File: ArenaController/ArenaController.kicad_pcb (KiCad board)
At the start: 2 copper layers, 80 x 110 mm, 30 parts, among them J1 RJ45, J2 RJ45, J4 RJ45, J5 RJ45, J6 RJ45, J8 Screw_Terminal_01x04, J9 Barrel_Jack_MountingPin, Q1 FS3400, Q2 FS3400, Q3 FS3400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

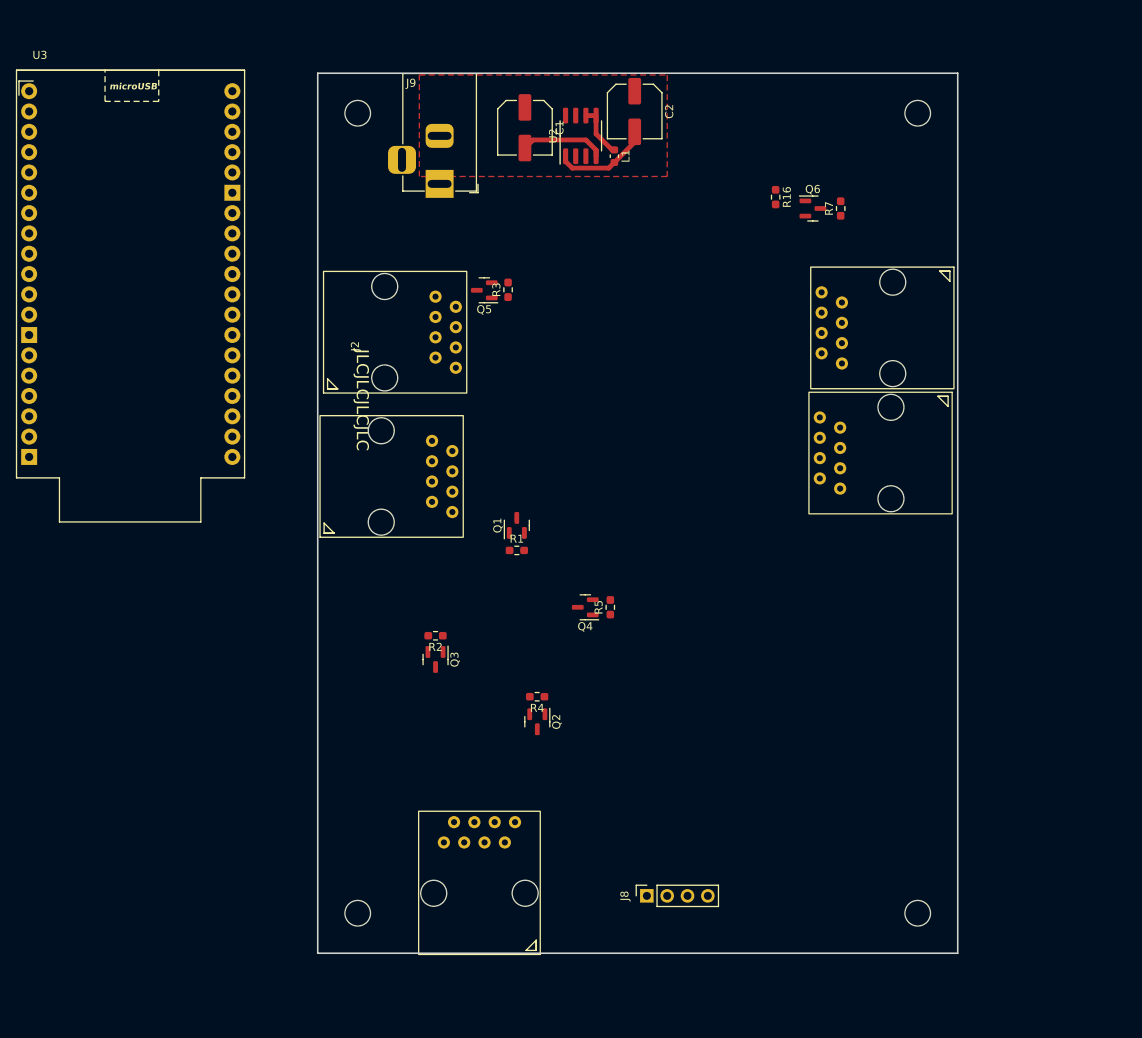
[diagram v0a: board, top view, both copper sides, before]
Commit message: Updated layout, added major routing.  Still need connector for the WS2812B output and pin relayout.
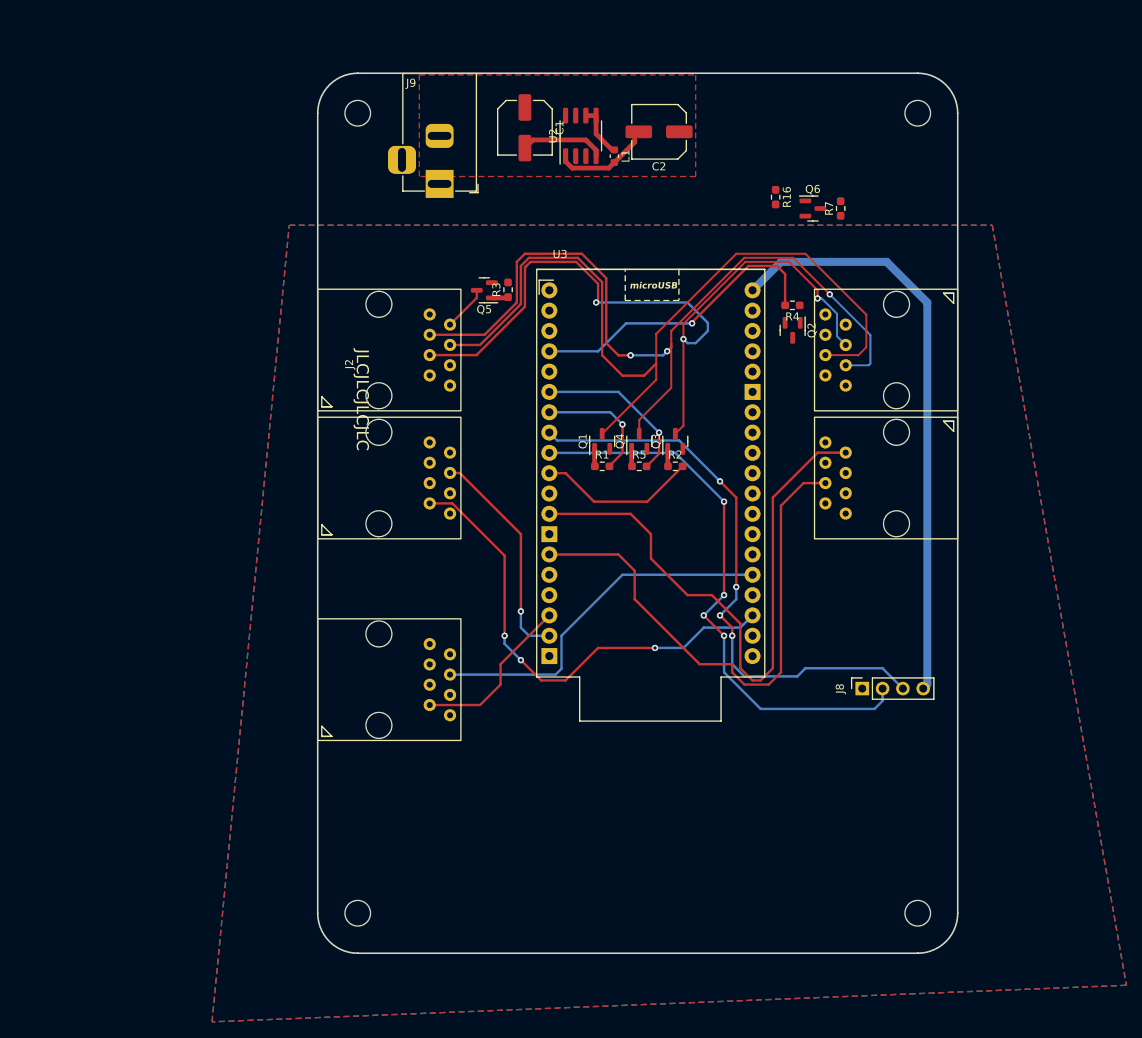
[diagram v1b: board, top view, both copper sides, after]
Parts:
- moved U3 69.6 mm to (136.7, 95.0)
- moved R4 58.4 mm to (154.3, 74.0)
- moved Q2 58.4 mm to (154.4, 77.1)
- moved Q3 40.5 mm to (139.7, 91.0), turned to 90 degrees
- moved J4 38.6 mm to (95.0, 128.4), turned to 90 degrees
- moved J8 37.4 mm to (163.1, 121.9)
- moved R2 36.7 mm to (139.7, 94.1), turned to 0 degrees
- moved kibuzzard-638A219C 36.5 mm to (97.8, 120.3), turned to 90 degrees
- moved Q4 21.8 mm to (135.2, 91.0), turned to 90 degrees
- moved J6 18.8 mm to (175.0, 88.0)
- moved R5 18.0 mm to (135.2, 94.1), turned to 0 degrees
- moved Q1 15.0 mm to (130.6, 91.0)
- moved R1 15.0 mm to (130.6, 94.1)
- moved J1 12.9 mm to (175.0, 72.0)
- moved C2 3.97 mm to (137.7, 52.3), turned to 180 degrees
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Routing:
- net /s_Green: track 0.00 -> 103.7 mm
- net /s_Yellow: track 0.00 -> 102.2 mm, vias 0 -> 3
- net /s_Horn: track 0.00 -> 96.6 mm, vias 0 -> 3
- net /T_A_End: track 0.00 -> 75.0 mm
- net +5V: track 12.3 -> 86.2 mm
- net /Dis_serial_Rx: track 0.00 -> 72.5 mm, vias 0 -> 4
- net /Dis_Serial_Tx: track 0.00 -> 71.5 mm, vias 0 -> 4
- net /T_A_Start: track 0.00 -> 66.5 mm
- net /T_B_Start: track 0.00 -> 59.3 mm, vias 0 -> 3
- net /G_Start: track 0.00 -> 45.4 mm
- net /m_Red_1: track 0.00 -> 38.3 mm, vias 0 -> 1
- net /T_B_End: track 0.00 -> 27.7 mm, vias 0 -> 1
- net /G_End: track 0.00 -> 21.1 mm
- net /m_Yellow: track 0.00 -> 20.7 mm, vias 0 -> 1
- net /m_Horn: track 0.00 -> 20.0 mm
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- added copper zone on B.Cu, net GND
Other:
- outline, holes or cut-outs redrawn

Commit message: Tiny cleanup, workable version, yay.
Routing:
- net +12V: track 10.6 -> 115.4 mm
- net +5V: track 86.2 -> 111.1 mm, vias 0 -> 1
- net /m_Red_2: track 0.00 -> 16.6 mm, vias 0 -> 1
- net /s_Green: track 103.7 -> 93.3 mm, vias 0 -> 2
- net /s_Horn: track 96.6 -> 90.8 mm, vias 3 -> 2
- net /m_Red_1: track 38.3 -> 42.5 mm, vias 1 -> 0
- net /s_Yellow: track 102.2 -> 98.7 mm, vias 3 -> 2
- net /m_Horn: track 20.0 -> 17.0 mm
- added copper zone on F.Cu, net +12V

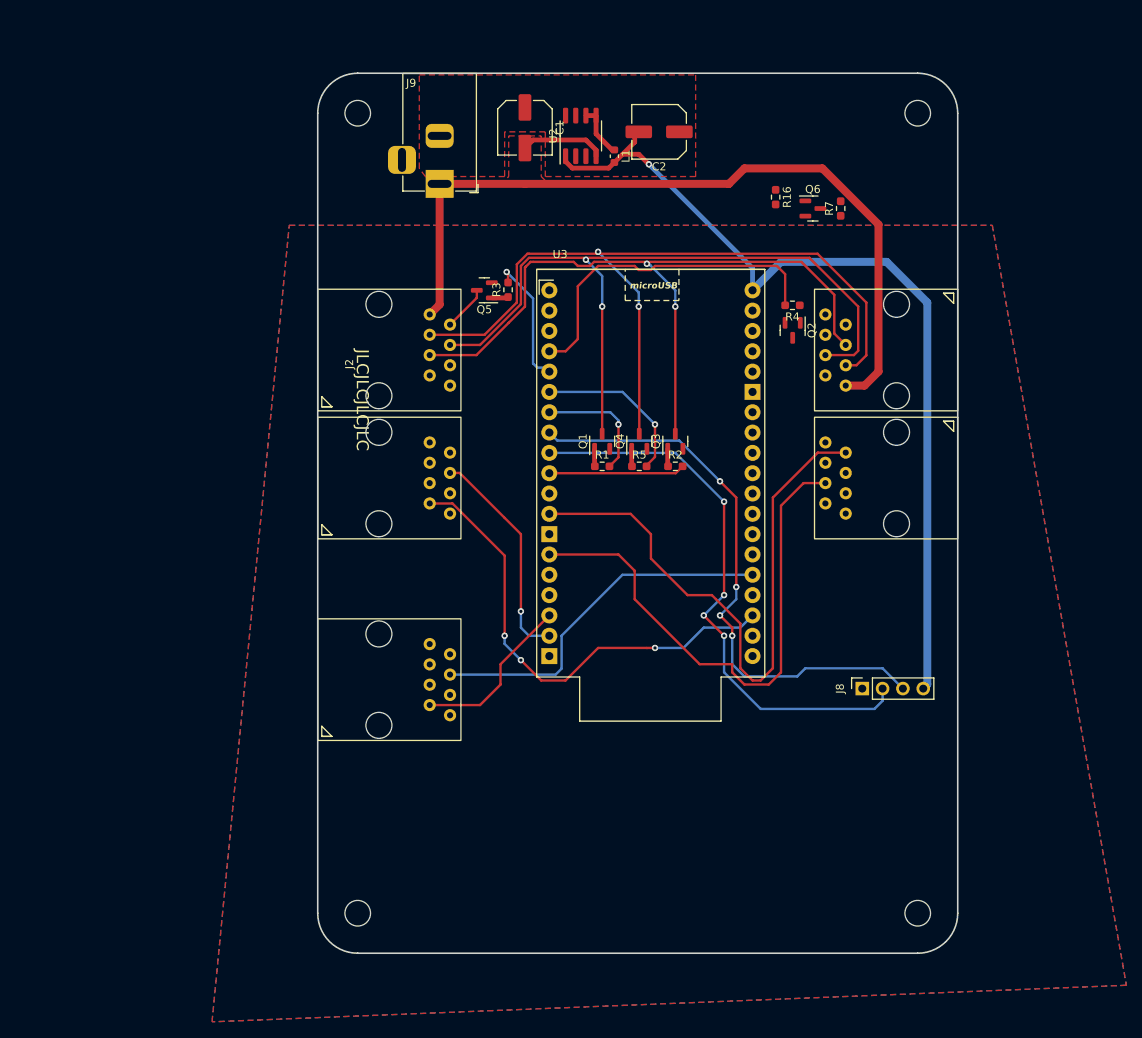
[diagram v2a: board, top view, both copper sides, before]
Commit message: Revision .4 layout with a sane ground plane, do fix the footprint shit tho
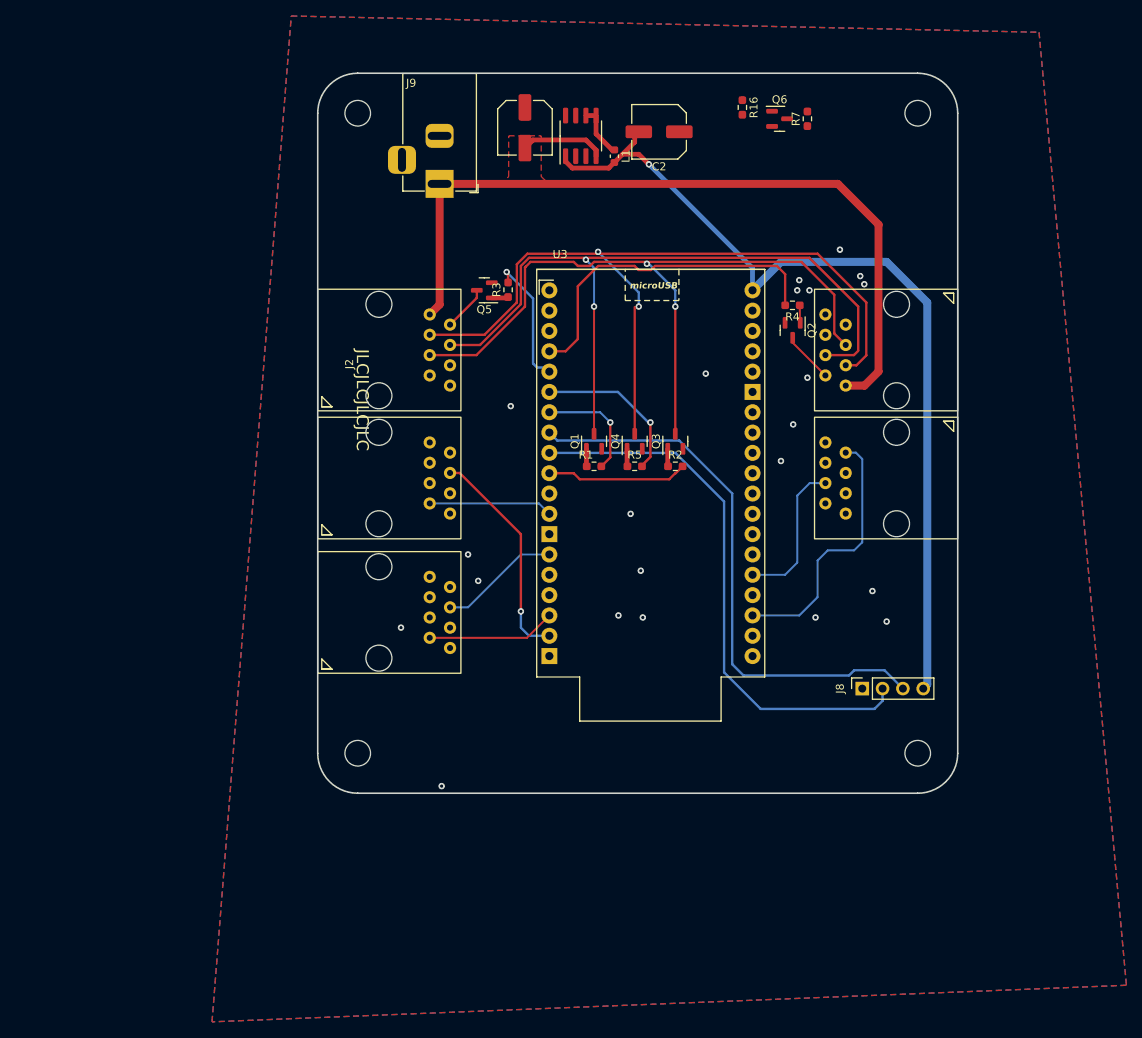
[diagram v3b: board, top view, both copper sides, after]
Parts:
- U2: value ~ -> XT4140
- moved H2 20.0 mm to (100.0, 130.0)
- moved H4 20.0 mm to (170.0, 130.0)
- moved Q6 12.0 mm to (152.7, 50.7)
- moved R16 12.0 mm to (148.1, 49.3)
- moved R7 12.0 mm to (156.2, 50.7)
- moved J4 8.40 mm to (95.0, 120.0)
- moved kibuzzard-638A219C 7.53 mm to (97.8, 112.8)
- moved Q1 1.02 mm to (129.5, 91.0)
- moved R1 1.02 mm to (129.5, 94.1)
- moved Q4 0.57 mm to (134.6, 91.0)
- moved R5 0.57 mm to (134.6, 94.1)
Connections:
- U3 pad 12: /T_A_End -> /T_B_Start
- U3 pad 14: /T_A_Start -> /G_Start
- U3 pad 22: /T_B_Start -> /T_A_End
- U3 pad 24: /G_Start -> /T_A_Start
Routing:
- net /T_A_Start: track 66.5 -> 18.8 mm
- net /T_B_Start: track 59.3 -> 15.5 mm, vias 3 -> 0
- net /T_A_End: track 75.0 -> 33.0 mm
- net /G_Start: track 45.4 -> 15.1 mm
- net +12V: track 115.4 -> 107.6 mm
- net /s_Red_1: track 0.00 -> 6.40 mm
- net /G_End: track 21.1 -> 16.1 mm
- net Net-(Q2-G): track 0.00 -> 2.21 mm
- net /Dis_Serial_Tx: track 71.5 -> 69.4 mm, vias 4 -> 0
- net /Dis_serial_Rx: track 72.5 -> 70.5 mm, vias 4 -> 0
- net /m_Green: track 15.3 -> 13.8 mm
- net /s_Horn: track 90.8 -> 90.1 mm
- net /m_Yellow: track 20.6 -> 19.9 mm
- net /m_Horn: track 17.0 -> 17.6 mm
- net GND: vias 0 -> 22
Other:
- board size 80 x 110 mm -> 80 x 90 mm
- board text added: "Arena Controller v.4 Kim Chase & Neil Flynn"
- board text added: "TRANS RIGHTS TRANS FIGHTS"

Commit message: Release v.4 for April event.
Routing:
- net +5V: track 111.1 -> 117.5 mm
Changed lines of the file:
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@@
   (gr_text "TRANS RIGHTS\nTRANS FIGHTS" (at 125.476 128.778) (layer "B.Mask")
     (effects (font (face "Sushi Sans") (size 2 2) (thickness 0.5) bold) (justify left bottom mirror))
-    (render_cache "TRANS RIGHTS\nTRANS FIGHTS" -0
+    (render_cache "TRANS RIGHTS\nTRANS FIGHTS" 0
       (polygon
         (pts
@@
   (segment (start 125.984 56.026416) (end 126.817084 56.8595) (width 0.6) (layer "F.Cu") (net 33))
   (via (at 136.398 56.388) (size 0.8) (drill 0.4) (layers "F.Cu" "B.Cu") (net 33))
-  (segment (start 149.352 72.136) (end 152.908 68.58) (width 1) (layer "B.Cu") (net 33))
   (segment (start 166.116 68.58) (end 171.196 73.66) (width 1) (layer "B.Cu") (net 33))
-  (segment (start 136.398 56.388) (end 149.352 69.342) (width 0.6) (layer "B.Cu") (net 33))
-  (segment (start 149.352 69.342) (end 149.352 72.136) (width 0.6) (layer "B.Cu") (net 33))
+  (segment (start 152.908 68.58) (end 149.606 68.58) (width 1) (layer "B.Cu") (net 33))
+  (segment (start 149.606 68.58) (end 149.352 68.834) (width 1) (layer "B.Cu") (net 33))
+  (segment (start 155.956 68.58) (end 166.116 68.58) (width 1) (layer "B.Cu") (net 33))
+  (segment (start 148.59 68.58) (end 149.606 68.58) (width 0.6) (layer "B.Cu") (net 33))
+  (segment (start 149.352 68.834) (end 149.352 72.136) (width 1) (layer "B.Cu") (net 33))
+  (segment (start 155.956 68.58) (end 148.59 68.58) (width 1) (layer "B.Cu") (net 33))
   (segment (start 171.196 121.412) (end 170.688 121.92) (width 1) (layer "B.Cu") (net 33))
-  (segment (start 152.908 68.58) (end 166.116 68.58) (width 1) (layer "B.Cu") (net 33))
+  (segment (start 152.908 68.58) (end 155.956 68.58) (width 1) (layer "B.Cu") (net 33))
   (segment (start 171.196 73.66) (end 171.196 121.412) (width 1) (layer "B.Cu") (net 33))
+  (segment (start 148.59 68.58) (end 136.398 56.388) (width 1) (layer "B.Cu") (net 33))
   (segment (start 114.8865 73.0785) (end 111.54 76.425) (width 0.3) (layer "F.Cu") (net 35))
   (segment (start 114.8865 72.136) (end 114.8865 73.0785) (width 0.3) (layer "F.Cu") (net 35))
